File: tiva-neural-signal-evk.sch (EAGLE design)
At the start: 34 parts, among them IC1 TM4C123G, IC2 TLV70233, X1 USB, X2 MICROSD, Y1 16MHz, Y2 32.768kHz

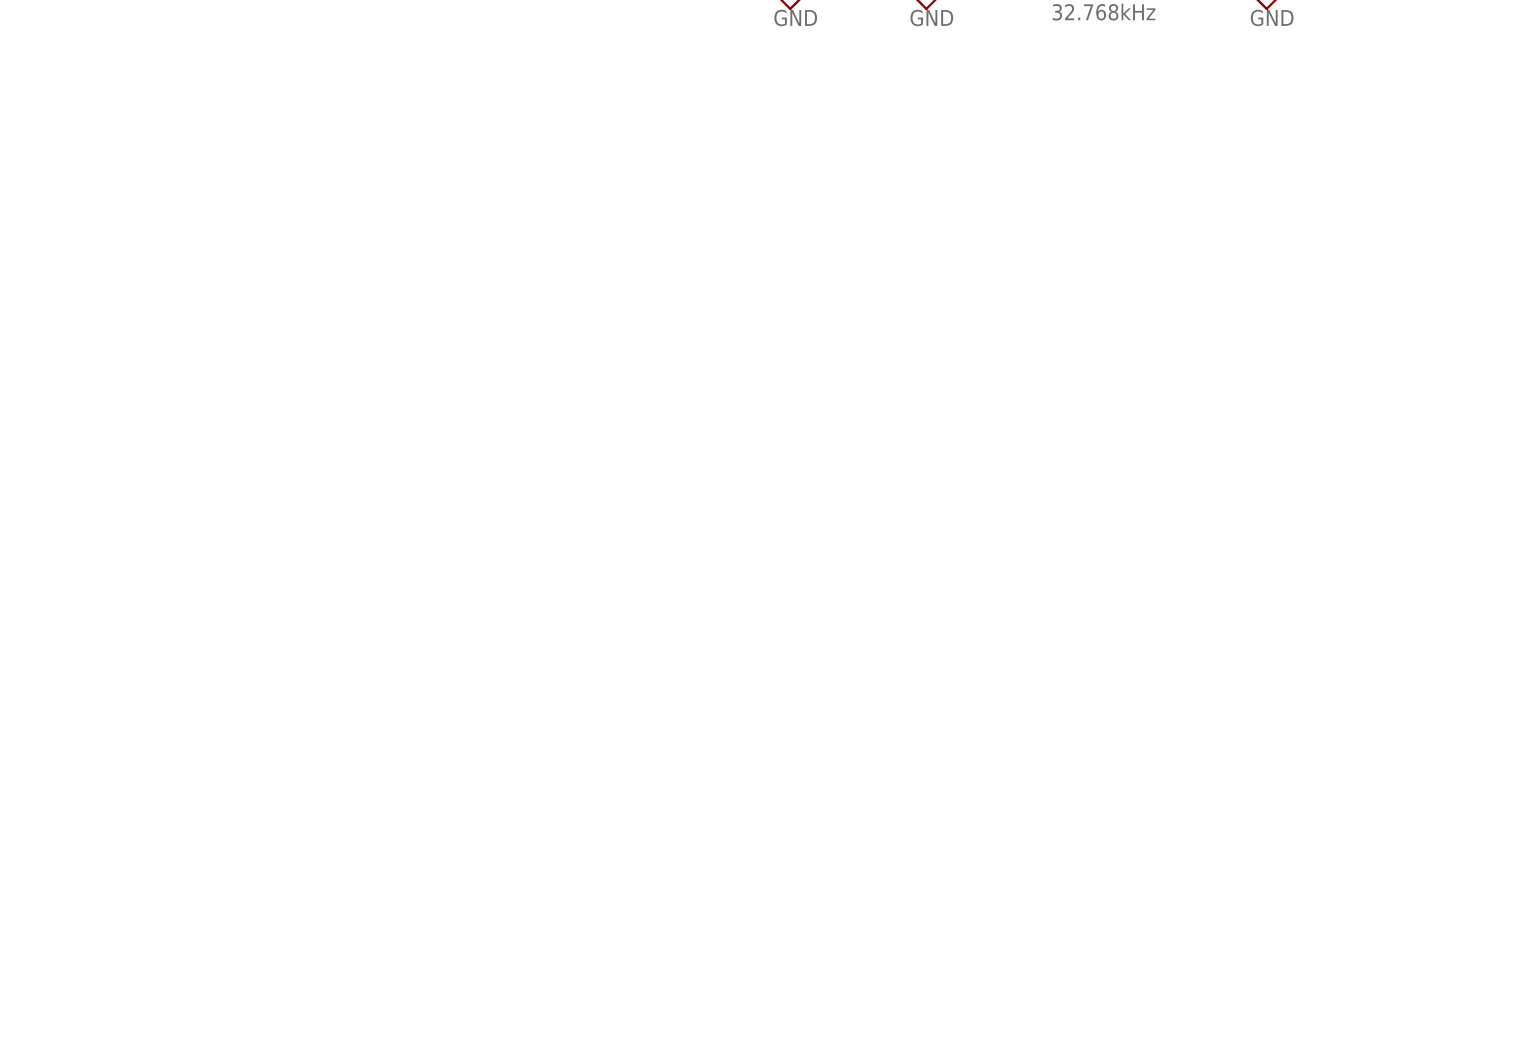
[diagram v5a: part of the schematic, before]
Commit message: added 2-ch instrumentation amp w/ op-amp gain stage
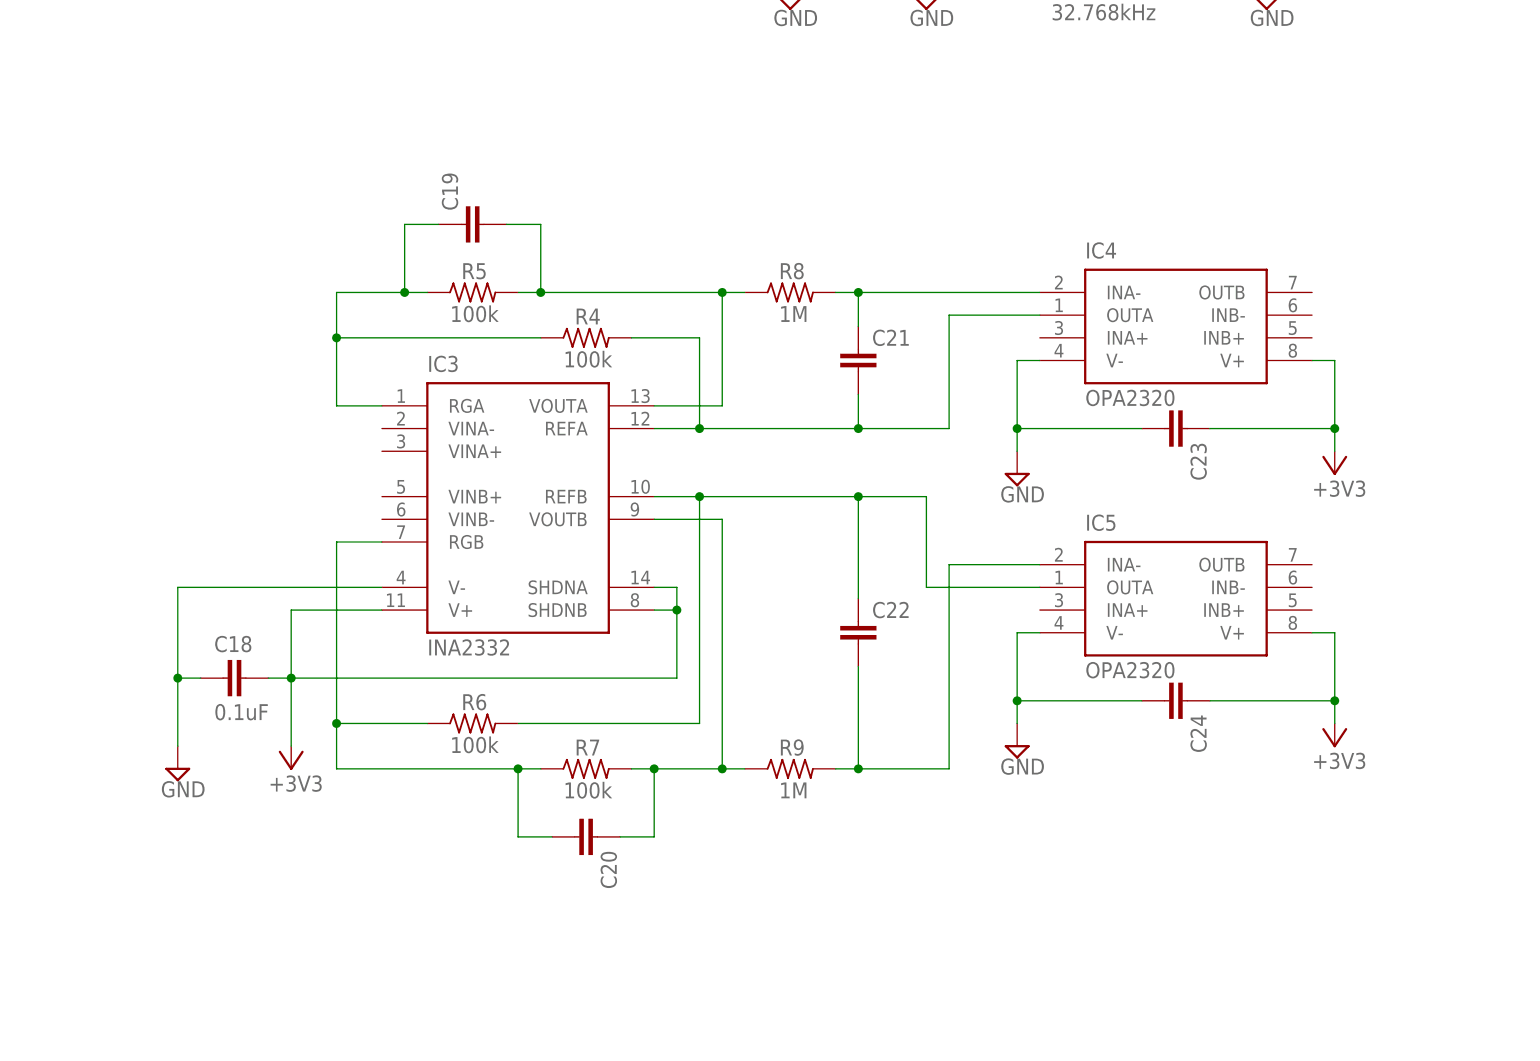
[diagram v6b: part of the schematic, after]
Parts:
- added C18: 0.1uF, rcl:C-EUC0603
- added C19, C20, C21, C22, C23, C24: (no value), rcl:C-EUC0603
- added IC3: INA2332, mor307:INA2332
- added IC4, IC5: OPA2320, mor307:OPA2320
- added R4, R5, R6, R7: 100k, rcl:R-US_R0603
- added R8, R9: 1M, rcl:R-US_R0603
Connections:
- new net N$1: C20.2, IC3.RGB, R6.1, R7.1
- new net N$12: C19.2, IC3.VOUTA, R5.2, R8.1
- new net N$14: C21.1, IC4.INA-, R8.2
- new net N$15: C22.2, IC5.INA-, R9.2
- new net N$2: C22.1, IC3.REFB, IC5.OUTA, R6.2
- new net N$3: C20.1, IC3.VOUTB, R7.2, R9.1
- new net N$4: C19.1, IC3.RGA, R4.1, R5.1
- new net N$5: C21.2, IC3.REFA, IC4.OUTA, R4.2
- net +3V3: now also C18.1, C23.1, C24.1, IC3.SHDNA, IC3.SHDNB, IC3.V+, IC4.V+, IC5.V+
- net GND: now also C18.2, C23.2, C24.2, IC3.V-, IC4.V-, IC5.V-

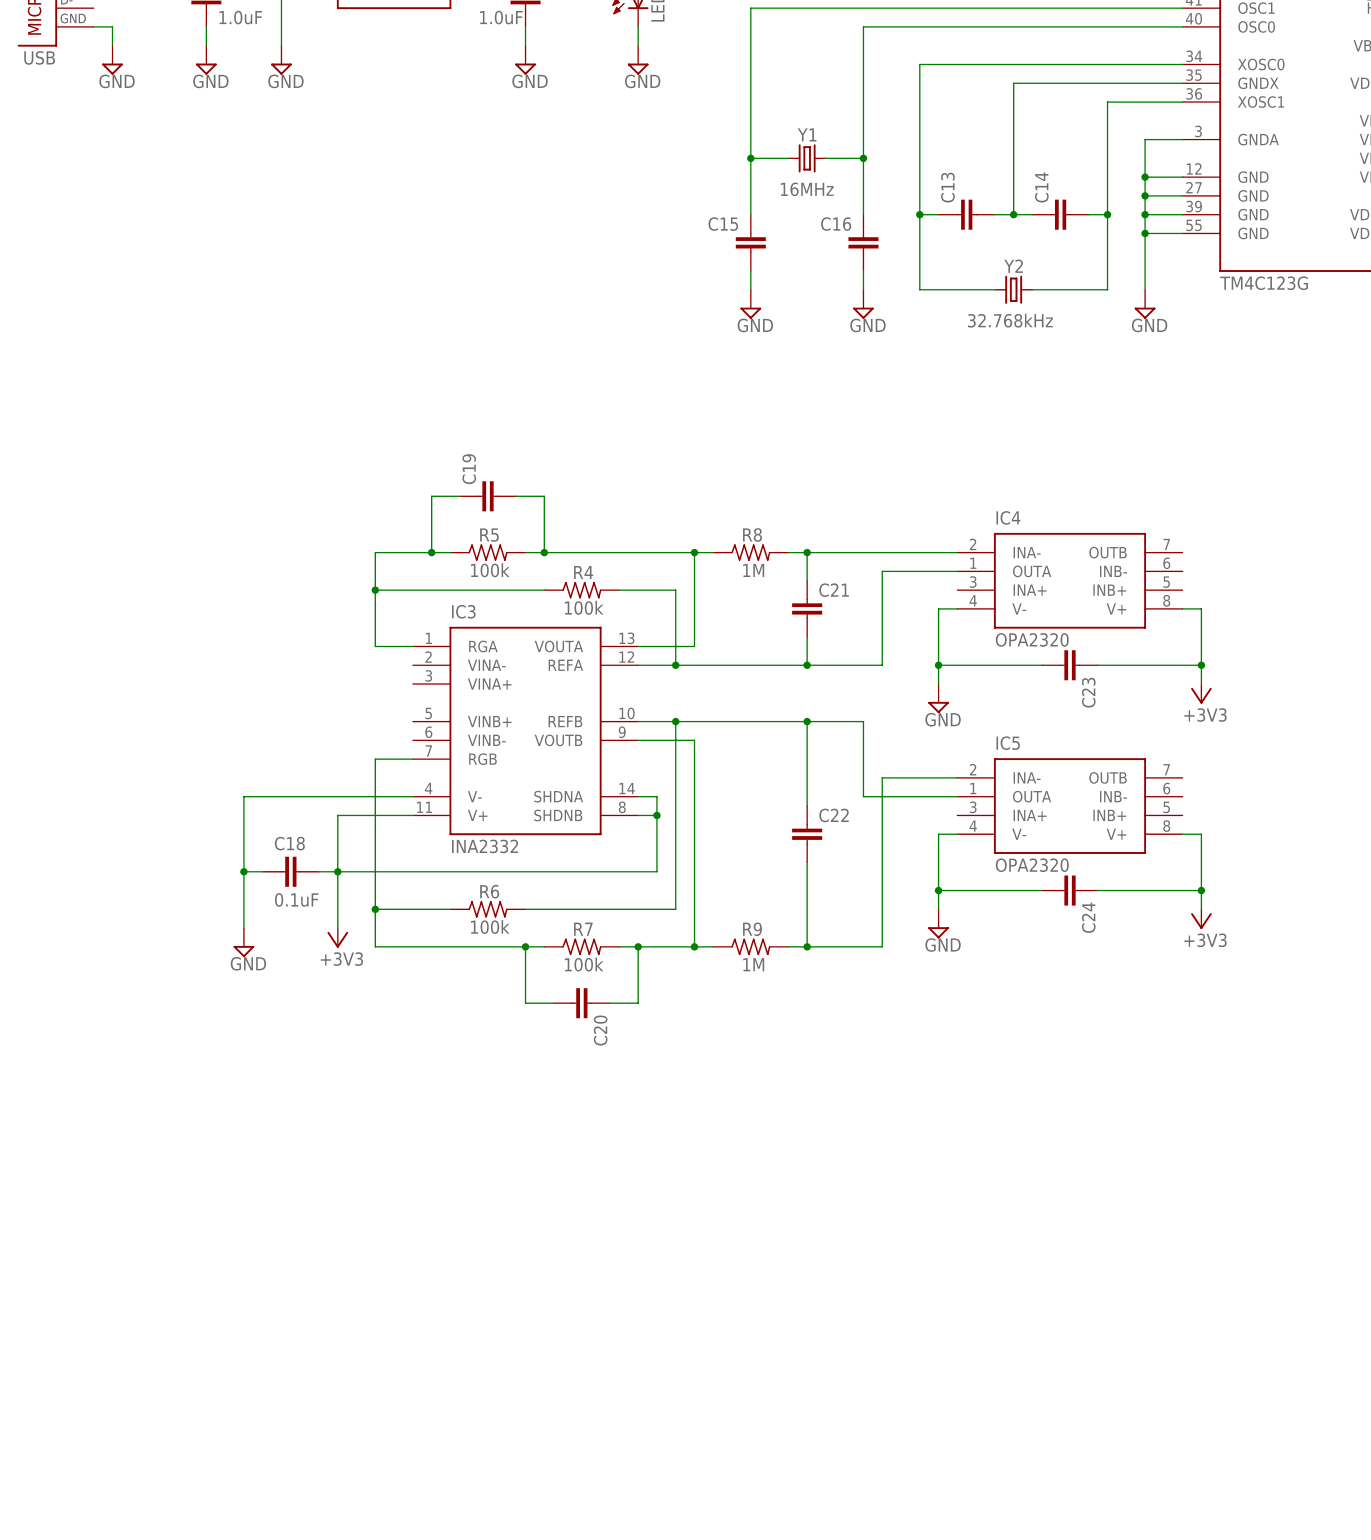
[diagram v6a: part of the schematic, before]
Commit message: added another 2-ch instrumentation amplifer
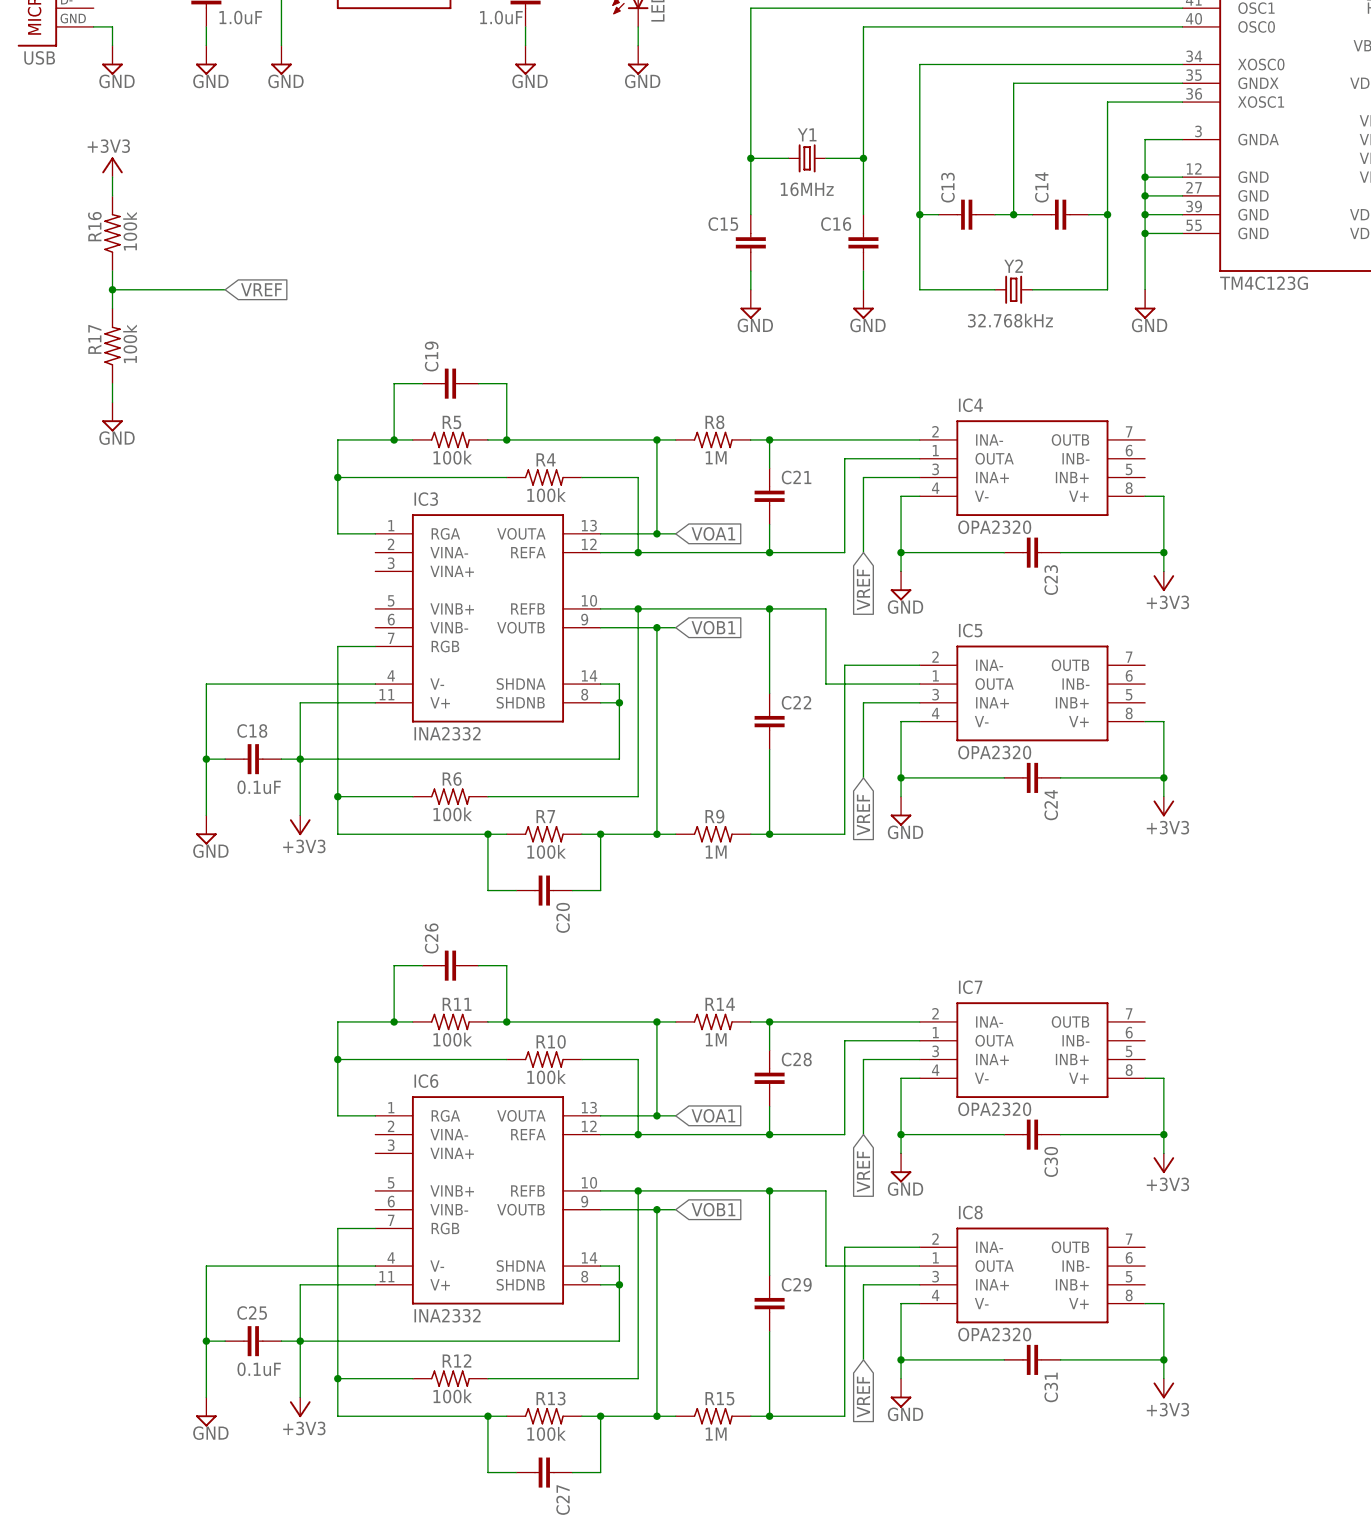
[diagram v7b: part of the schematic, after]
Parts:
- added C25: 0.1uF, rcl:C-EUC0603
- added C26, C27, C28, C29, C30, C31: (no value), rcl:C-EUC0603
- added IC6: INA2332, mor307:INA2332
- added IC7, IC8: OPA2320, mor307:OPA2320
- added R10, R11, R12, R13, R16, R17: 100k, rcl:R-US_R0603
- added R14, R15: 1M, rcl:R-US_R0603
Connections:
- new net N$13: C27.2, IC6.RGB, R12.1, R13.1
- new net N$16: C29.1, IC6.REFB, IC8.OUTA, R12.2
- new net N$17: C28.1, IC7.INA-, R14.2
- new net N$18: C29.2, IC8.INA-, R15.2
- new net VOA1: C19.2, C26.2, IC3.VOUTA, IC6.VOUTA, R11.2, R14.1, R5.2, R8.1
- new net VOB1: C20.1, C27.1, IC3.VOUTB, IC6.VOUTB, R13.2, R15.1, R7.2, R9.1
- new net VREF: IC4.INA+, IC5.INA+, IC7.INA+, IC8.INA+, R16.1, R17.2
- net +3V3: now also C25.1, C30.1, C31.1, IC6.SHDNA, IC6.SHDNB, IC6.V+, IC7.V+, IC8.V+, R16.2
- net GND: now also C25.2, C30.2, C31.2, IC6.V-, IC7.V-, IC8.V-, R17.1
- net N$12: now also C28.2, IC6.REFA, IC7.OUTA, R10.2; no longer C19.2, IC3.VOUTA, R5.2, R8.1
- net N$3: now also C26.1, IC6.RGA, R10.1, R11.1; no longer C20.1, IC3.VOUTB, R7.2, R9.1
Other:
- moved on the sheet: C18, C19, C20, C21, C22, C23, C24, IC3, IC4, IC5, R4, R5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
